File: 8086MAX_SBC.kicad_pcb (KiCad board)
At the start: 4 copper layers, 270.8 x 145 mm, 114 parts, among them J1 ATX POWER, J2 Conn_02x05_Odd_Even, J3 Conn_02x08_Odd_Even, J4 Conn_02x08_Odd_Even, J5 GPIO, J6 Bus_ISA_8bit, J7 Conn_02x17_Odd_Even, J8 TTL UART, SW1 SW_SPST, SW2 SW_Push, U1 74HC14, U10 SST39SF040, U11 SST39SF040, U12 8086_Max_Mode, U13 8284, U14 8087, U15 8089, U16 80130-6, U17 8288, U18 8289, U19 74LS573, U2 74HCT74, U20 74LS245, U21 74LS573, U22 74LS245, U23 74LS573, U24 74LS06, U25 SN74LS07N, U26 74LS273, U27 74LS273, U28 74LS244, U29 74LS244, U3 74164, U30 74LS32, U31 TXS0104ED, U32 16550, U33 WD37C65, U34 74HC00, U6 74164, U7 AS6C4008-55PCN, U8 AS6C4008-55PCN, U9 ATF1508AS-10JU84, Y1 15MHz, Y2 9.6 MHz, Y3 16 MHz

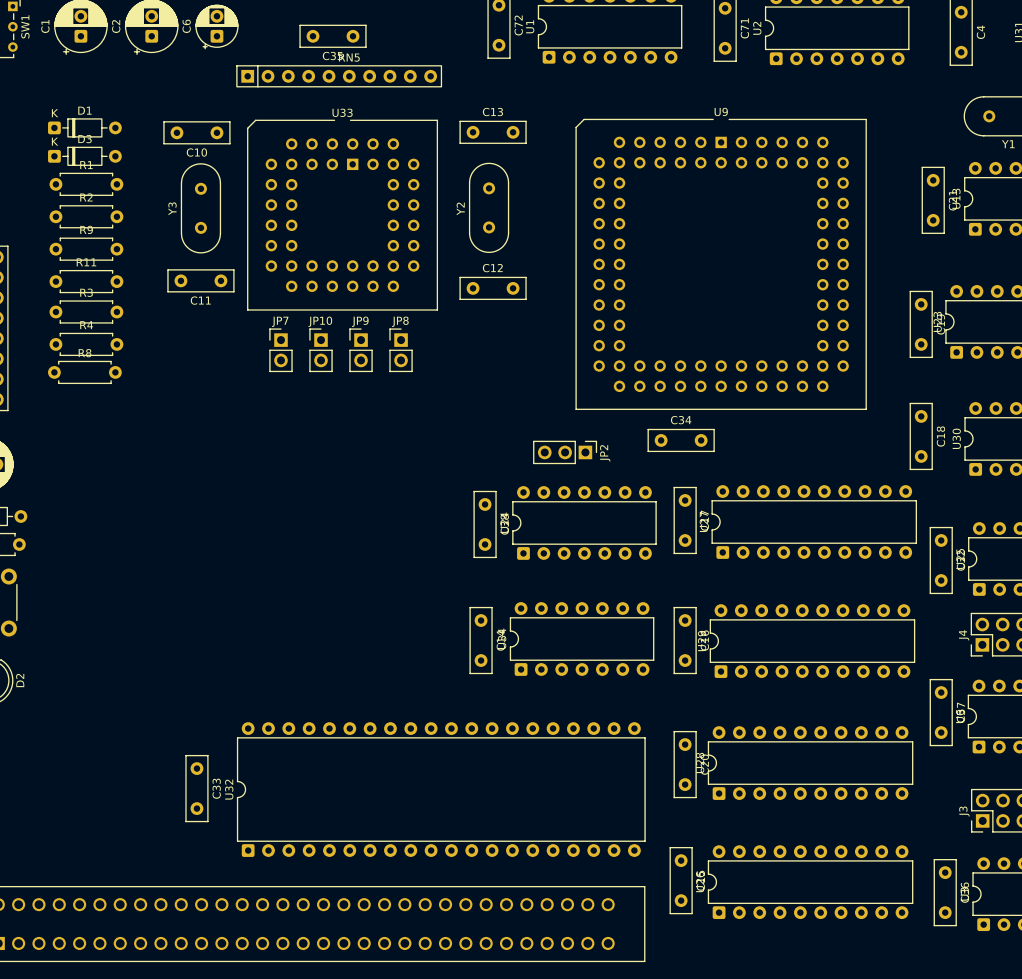
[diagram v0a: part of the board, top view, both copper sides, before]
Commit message: Fixed some silkscreen overlap
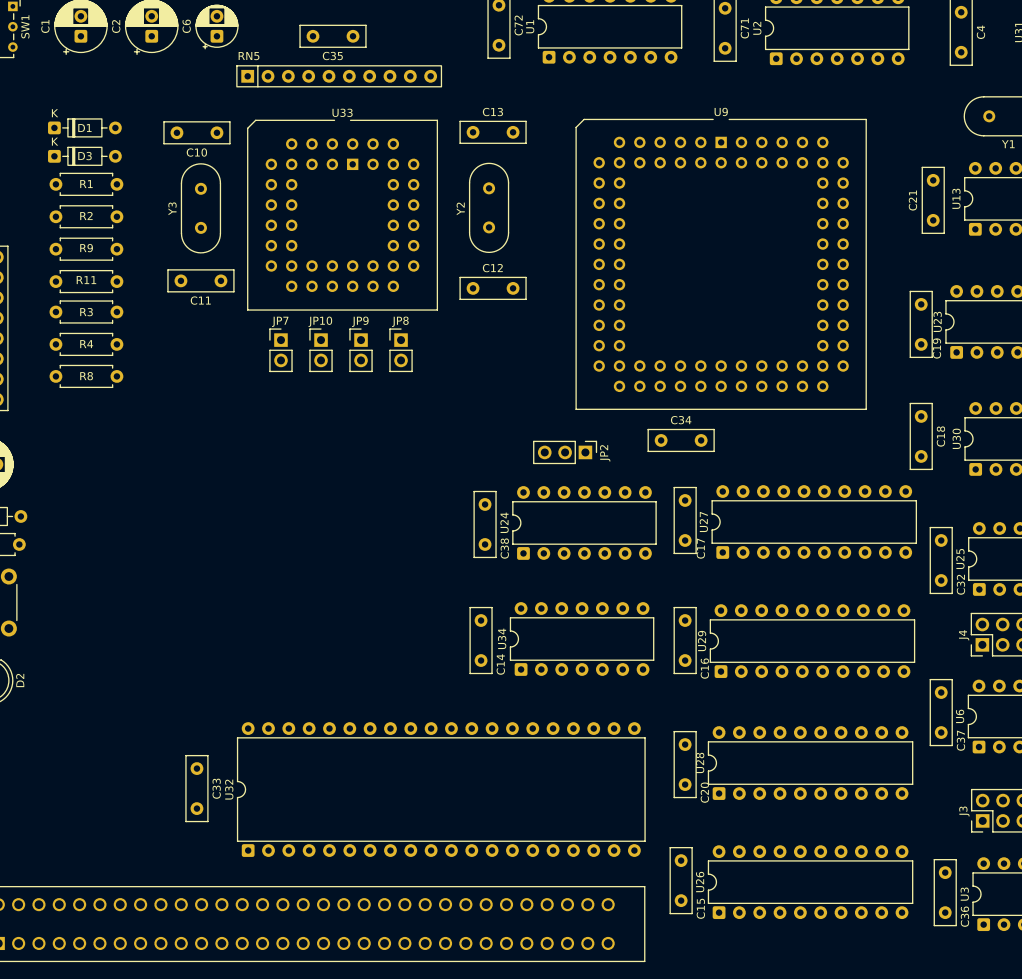
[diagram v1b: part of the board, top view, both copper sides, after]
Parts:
- moved R8 0.53 mm to (31.4, 82.0)
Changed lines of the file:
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@@
 		(tags "Diode DO-35_SOD27 series Axial Horizontal pin pitch 7.62mm  length 4mm diameter 2mm")
 		(property "Reference" "D3"
-			(at 3.81 -2.12 0)
+			(at 3.81 0 0)
 			(layer "F.SilkS")
 			(effects
@@
 		(tags "C Disc series Radial pin pitch 5.00mm diameter 8mm width 2.5mm Capacitor")
 		(property "Reference" "C32"
-			(at 2.5 -2.5 90)
+			(at 5.5 -2.5 90)
 			(layer "F.SilkS")
 			(effects
@@
 		(tags "C Disc series Radial pin pitch 5.00mm diameter 8mm width 2.5mm Capacitor")
 		(property "Reference" "C15"
-			(at 2.5 -2.5 90)
+			(at 6 -2.5 90)
 			(layer "F.SilkS")
 			(effects
@@
 		(tags "R")
 		(property "Reference" "RN5"
-			(at 12.7 -2.31 0)
+			(at 0.16 -2.5 0)
 			(layer "F.SilkS")
 			(effects
@@
 		(tags "C Disc series Radial pin pitch 5.00mm diameter 8mm width 2.5mm Capacitor")
 		(property "Reference" "C37"
-			(at 2.5 -2.5 90)
+			(at 6 -2.5 90)
 			(layer "F.SilkS")
 			(effects
@@
 		(tags "Resistor Axial_DIN0207 series Axial Horizontal pin pitch 7.62mm 0.25W = 1/4W length 6.3mm diameter 2.5mm")
 		(property "Reference" "R3"
-			(at 3.81 -2.37 0)
+			(at 3.81 0.05 0)
 			(layer "F.SilkS")
 			(effects
@@
 		(tags "Resistor Axial_DIN0207 series Axial Horizontal pin pitch 7.62mm 0.25W = 1/4W length 6.3mm diameter 2.5mm")
 		(property "Reference" "R4"
-			(at 3.81 -2.37 0)
+			(at 3.81 0 0)
 			(layer "F.SilkS")
 			(effects
@@
 		(tags "Resistor Axial_DIN0207 series Axial Horizontal pin pitch 7.62mm 0.25W = 1/4W length 6.3mm diameter 2.5mm")
 		(property "Reference" "R9"
-			(at 3.81 -2.37 0)
+			(at 3.81 -0.1 0)
 			(layer "F.SilkS")
 			(effects
@@
 		(tags "C Disc series Radial pin pitch 5.00mm diameter 8mm width 2.5mm Capacitor")
 		(property "Reference" "C14"
-			(at 2.5 -2.5 90)
+			(at 5.5 -2.5 90)
 			(layer "F.SilkS")
 			(effects
@@
 	(footprint "Resistor_THT:R_Axial_DIN0207_L6.3mm_D2.5mm_P7.62mm_Horizontal"
 		(layer "F.Cu")
-		(at 31.19 81.5)
+		(at 31.38 82)
 		(descr "Resistor, Axial_DIN0207 series, Axial, Horizontal, pin pitch=7.62mm, 0.25W = 1/4W, length*diameter=6.3*2.5mm^2, http://cdn-reichelt.de/documents/datenblatt/B400/1_4W%23YAG.pdf")
 		(tags "Resistor Axial_DIN0207 series Axial Horizontal pin pitch 7.62mm 0.25W = 1/4W length 6.3mm diameter 2.5mm")
 		(property "Reference" "R8"
-			(at 3.81 -2.37 0)
+			(at 3.81 0 0)
 			(layer "F.SilkS")
 			(effects
@@
 		(tags "C Disc series Radial pin pitch 5.00mm diameter 8mm width 2.5mm Capacitor")
 		(property "Reference" "C19"
-			(at 2.5 -2.5 90)
+			(at 5.5 -2 90)
 			(layer "F.SilkS")
 			(effects
@@
 		(tags "C Disc series Radial pin pitch 5.00mm diameter 8mm width 2.5mm Capacitor")
 		(property "Reference" "C17"
-			(at 2.5 -2.5 90)
+			(at 6 -2 90)
 			(layer "F.SilkS")
 			(effects
@@
 		(tags "C Disc series Radial pin pitch 5.00mm diameter 8mm width 2.5mm Capacitor")
 		(property "Reference" "C16"
-			(at 2.5 -2.5 90)
+			(at 6 -2.5 90)
 			(layer "F.SilkS")
 			(effects
@@
 		(tags "C Disc series Radial pin pitch 5.00mm diameter 8mm width 2.5mm Capacitor")
 		(property "Reference" "C36"
-			(at 2.5 -2.5 90)
+			(at 5.5 -2.5 90)
 			(layer "F.SilkS")
 			(effects
@@
 		(tags "C Disc series Radial pin pitch 5.00mm diameter 8mm width 2.5mm Capacitor")
 		(property "Reference" "C21"
-			(at 2.5 -2.5 90)
+			(at 2.5 2.5 90)
 			(layer "F.SilkS")
 			(effects
@@
 		(tags "Diode DO-35_SOD27 series Axial Horizontal pin pitch 7.62mm  length 4mm diameter 2mm")
 		(property "Reference" "D1"
-			(at 3.81 -2.12 0)
+			(at 3.81 0.05 0)
 			(layer "F.SilkS")
 			(effects
@@
 		(tags "Resistor Axial_DIN0207 series Axial Horizontal pin pitch 7.62mm 0.25W = 1/4W length 6.3mm diameter 2.5mm")
 		(property "Reference" "R1"
-			(at 3.81 -2.37 0)
+			(at 3.81 0 0)
 			(layer "F.SilkS")
 			(effects
@@
 		(tags "C Disc series Radial pin pitch 5.00mm diameter 8mm width 2.5mm Capacitor")
 		(property "Reference" "C38"
-			(at 2.5 -2.5 90)
+			(at 5.5 -2.5 90)
 			(layer "F.SilkS")
 			(effects
@@
 		(tags "C Disc series Radial pin pitch 5.00mm diameter 8mm width 2.5mm Capacitor")
 		(property "Reference" "C20"
-			(at 2.5 -2.5 90)
+			(at 6 -2.5 90)
 			(layer "F.SilkS")
 			(effects
@@
 		(tags "Resistor Axial_DIN0207 series Axial Horizontal pin pitch 7.62mm 0.25W = 1/4W length 6.3mm diameter 2.5mm")
 		(property "Reference" "R11"
-			(at 3.81 -2.37 0)
+			(at 3.81 -0.15 0)
 			(layer "F.SilkS")
 			(effects
@@
 		(tags "Resistor Axial_DIN0207 series Axial Horizontal pin pitch 7.62mm 0.25W = 1/4W length 6.3mm diameter 2.5mm")
 		(property "Reference" "R2"
-			(at 3.81 -2.37 0)
+			(at 3.81 -0.05 0)
 			(layer "F.SilkS")
 			(effects

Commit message: Fixed missing nets
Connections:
- U15 pad 10: unconnected-(U15-AD6-Pad10) -> AD6
- U15 pad 11: unconnected-(U15-AD5-Pad11) -> AD5
- U15 pad 12: unconnected-(U15-AD4-Pad12) -> AD4
- U15 pad 13: unconnected-(U15-AD3-Pad13) -> AD3
- U15 pad 14: unconnected-(U15-AD2-Pad14) -> AD2
- U15 pad 15: unconnected-(U15-AD1-Pad15) -> AD1
- U15 pad 16: unconnected-(U15-AD0-Pad16) -> AD0
- U15 pad 2: unconnected-(U15-AD14-Pad2) -> AD14
- U15 pad 3: unconnected-(U15-AD13-Pad3) -> AD13
- U15 pad 32: unconnected-(U15-EXT_2-Pad32) -> 8089EXT2
- U15 pad 33: unconnected-(U15-EXT_1-Pad33) -> 8089EXT1
- U15 pad 35: unconnected-(U15-A19/S6-Pad35) -> AD19
- U15 pad 36: unconnected-(U15-A18/S5-Pad36) -> AD18
- U15 pad 37: unconnected-(U15-A17/S4-Pad37) -> AD17
- U15 pad 38: unconnected-(U15-A16/S3-Pad38) -> AD16
- U15 pad 39: unconnected-(U15-AD15-Pad39) -> AD15
- U15 pad 4: unconnected-(U15-AD12-Pad4) -> AD12
- U15 pad 5: unconnected-(U15-AD11-Pad5) -> AD11
- U15 pad 6: unconnected-(U15-AD10-Pad6) -> AD10
- U15 pad 7: unconnected-(U15-AD9-Pad7) -> AD9
- U15 pad 8: unconnected-(U15-AD8-Pad8) -> AD8
- U15 pad 9: unconnected-(U15-AD7-Pad9) -> AD7
- U16 pad 26: unconnected-(U16-~{S0}-Pad26) -> ~{S0}
- U16 pad 27: unconnected-(U16-~{S1}-Pad27) -> ~{S1}
- U16 pad 28: unconnected-(U16-~{S2}-Pad28) -> ~{S2}
- U9 pad 63: unconnected-(U9-I/O-Pad63) -> 8089EXT2
- U9 pad 64: unconnected-(U9-I/O-Pad64) -> GND
- U9 pad 65: unconnected-(U9-I/O-Pad65) -> GND
- U9 pad 67: unconnected-(U9-I/O-Pad67) -> 8089EXT1
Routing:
- net GND: track 0.00 -> 40.6 mm

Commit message: Minor changes to ground
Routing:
- net GND: track 40.6 -> 60.5 mm
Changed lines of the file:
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@@
+	)
+	(segment
+		(start 73.54 63.12)
+		(end 69.8888 66.7712)
+		(width 0.4)
+		(layer "F.Cu")
+		(net 1)
+	)
+	(segment
+		(start 59.7288 66.7712)
+		(end 58.3 68.2)
+		(width 0.4)
+		(layer "F.Cu")
+		(net 1)
 	)
 	(segment
@@
 		(width 2)
 		(layer "F.Cu")
+		(net 1)
+	)
+	(segment
+		(start 69.8888 66.7712)
+		(end 59.7288 66.7712)
+		(width 0.4)
+		(layer "F.Cu")
+		(net 1)
+	)
+	(segment
+		(start 127.2 68)
+		(end 129.74 68)
+		(width 2)
+		(layer "F.Cu")

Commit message: Finished routing traces
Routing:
- net GND: track 60.5 -> 2189.7 mm, vias 0 -> 11
- net 5V-18: track 0.00 -> 787.9 mm, vias 0 -> 3
- net 5V-7: track 0.00 -> 722.0 mm, vias 0 -> 17
- net D1: track 0.00 -> 436.7 mm, vias 0 -> 7
- net CLK: track 0.00 -> 423.6 mm, vias 0 -> 4
- net ~{MRDC}: track 0.00 -> 422.8 mm, vias 0 -> 4
- net RESET: track 0.00 -> 421.3 mm, vias 0 -> 3
- net D0: track 0.00 -> 420.2 mm, vias 0 -> 6
- net D2: track 0.00 -> 418.7 mm, vias 0 -> 6
- net D3: track 0.00 -> 416.1 mm, vias 0 -> 4
- net D4: track 0.00 -> 407.3 mm, vias 0 -> 4
- net 5V-11: track 0.00 -> 403.0 mm, vias 0 -> 1
- net D7: track 0.00 -> 402.3 mm, vias 0 -> 3
- net D5: track 0.00 -> 397.6 mm, vias 0 -> 2
- net ~{MWTC}: track 0.00 -> 386.1 mm, vias 0 -> 7
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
